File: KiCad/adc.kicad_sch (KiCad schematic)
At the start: 32 parts, among them U901 AP331, U902 74LVC2G53

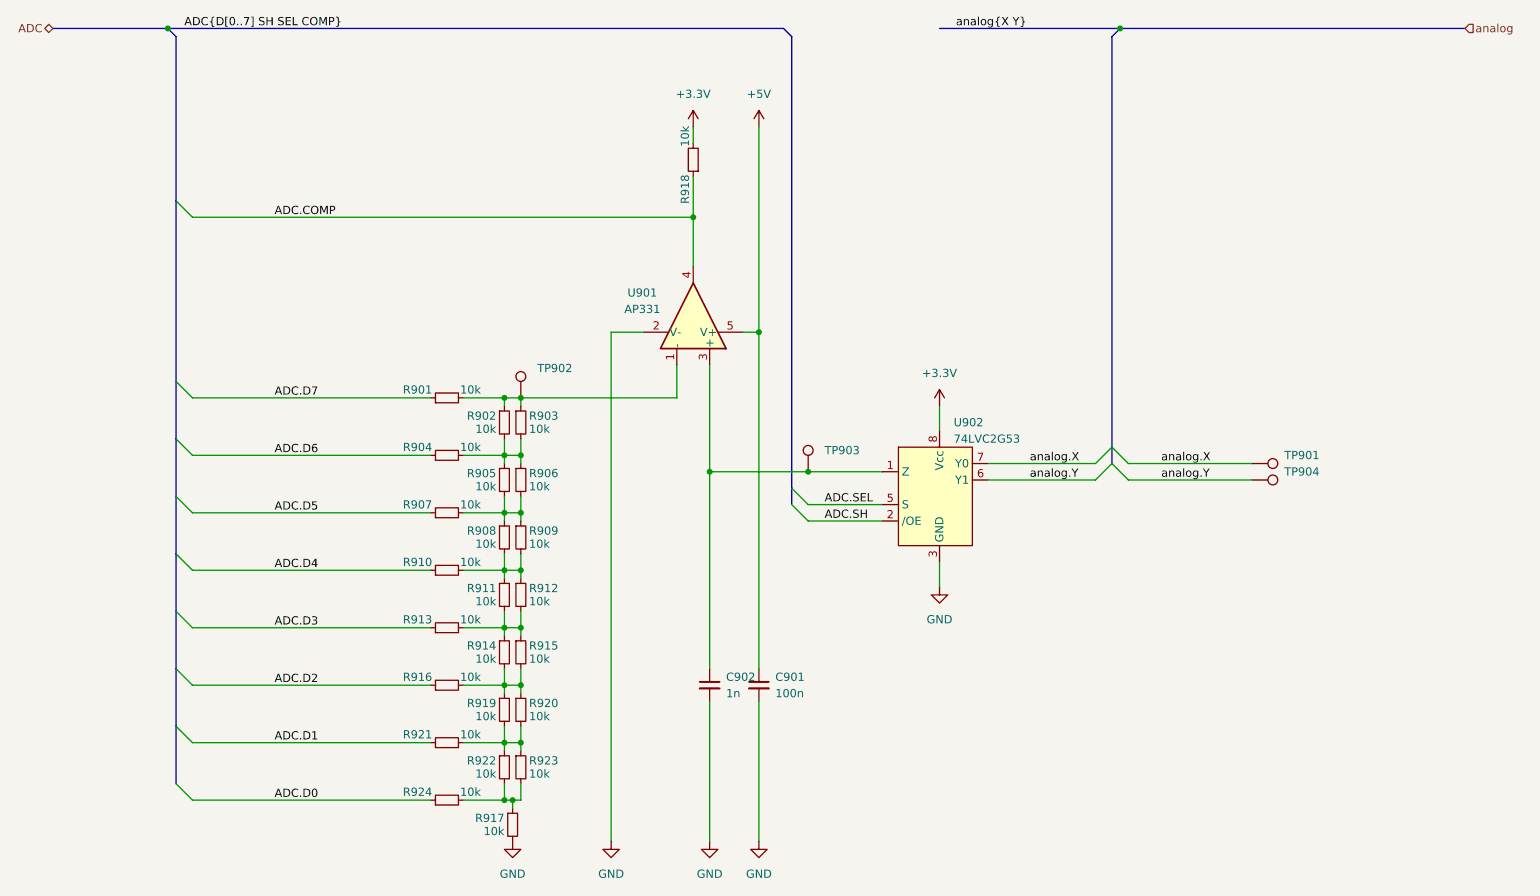
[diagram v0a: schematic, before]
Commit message: replaced SAR-ADC with Sigma-Delta-Converter
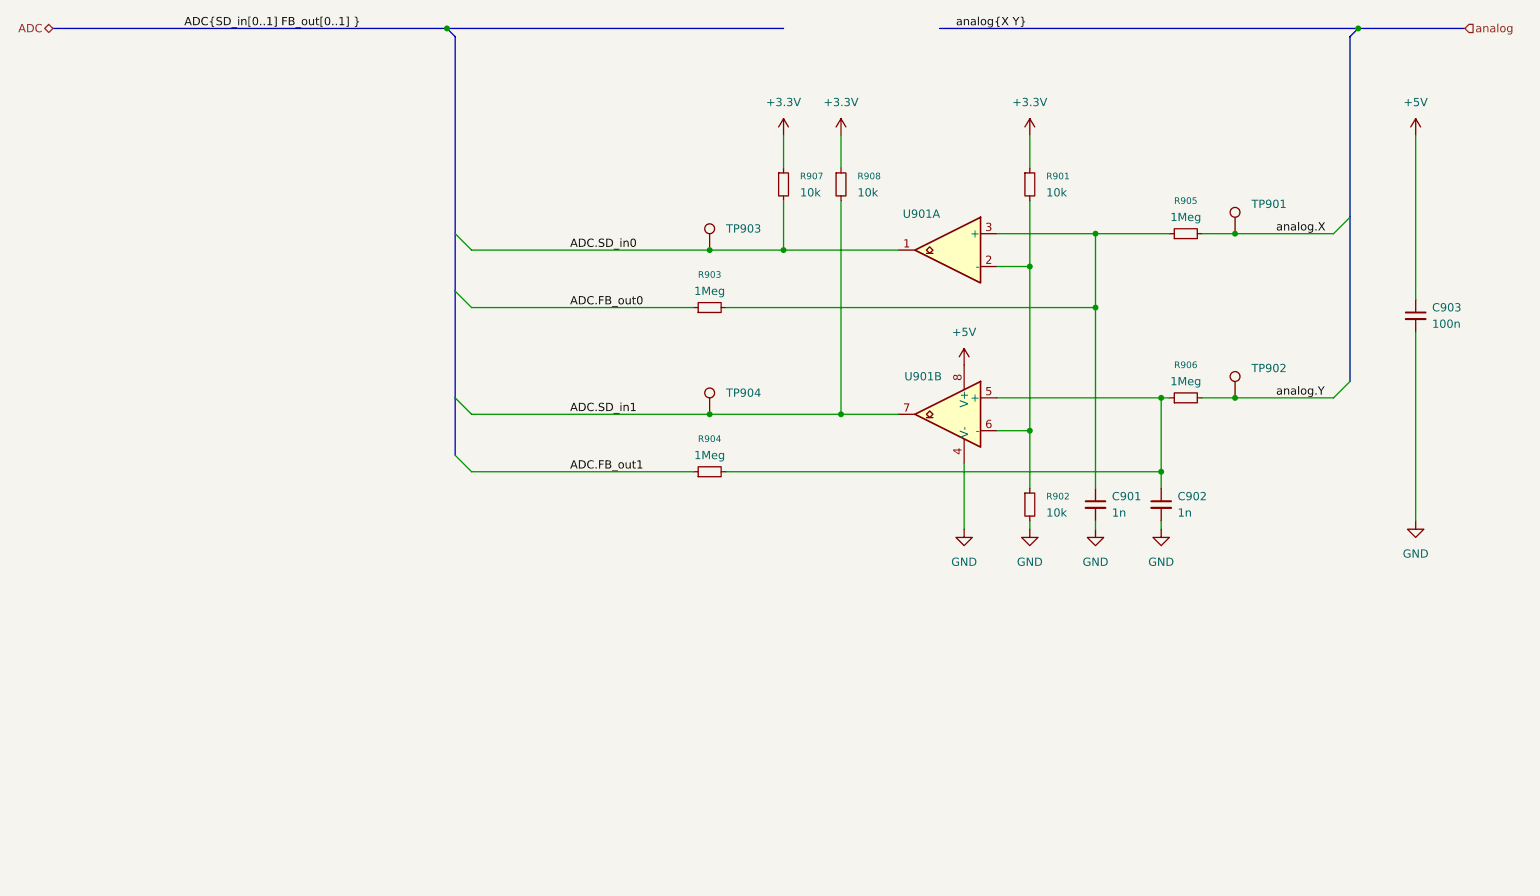
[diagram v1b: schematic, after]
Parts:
- removed R909, R910, R911, R912, R913, R914, R915, R916, R917, R918, R919, R920, R921, R922, R923, R924: 10k, Resistor_SMD:R_0402_1005Metric, symbol Device:R_Small
- removed U901: AP331, Package_TO_SOT_SMD:SOT-23-5, symbol Comparator:LM397
- removed U902: 74LVC2G53, Package_SO:VSSOP-8_2.4x2.1mm_P0.5mm, symbol FPGA-Devel:74LVC2G53
- added C903: 100n, Capacitor_SMD:C_0402_1005Metric, symbol Device:C_Small
- added U901: LM2903, Package_SO:VSSOP-8_3x3mm_P0.65mm, symbol Comparator:LM2903
- C901: value 100n -> 1n; Würth 885012205037 -> (none)
- C902: Würth 885012205025 -> (none)
- R901, R902, R907, R908: Würth 560112110020 -> (none)
- R903, R904, R905, R906: value 10k -> 1Meg; Würth 560112110020 -> (none)
- TP901, TP902, TP903, TP904: Würth - -> (none)
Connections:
- net ADC.D5 is gone; now on net +3.3V: R907.1
- net ADC.D7 is gone; now on net +3.3V: R901.1
- net +3.3V: now also R908.1
- net +5V: now also C903.1, U901.8 (V+); no longer C901.1
- net GND: now also R902.2, C903.2, U901.4 (V-)
- net analog.X: now also R905.2
- net analog.Y: now also R906.2, TP902.1; no longer TP904.1
- net at C902.1: now also R904.2, R906.1, U901.5 (+); no longer TP903.1
- net at R901.2, R902.1: now also U901.2 (-), U901.6 (-); no longer R903.1, TP902.1
- net ADC.SD_in1: now reaches R908.2
- net ADC.SD_in1: now also TP904.1, U901.7
- net ADC.D6 renamed ADC.FB_out1
- new net: C901.1, R903.2, R905.1, U901.3 (+)
- new net ADC.FB_out0: R903.1
- new net ADC.SD_in0: R907.2, TP903.1, U901.1

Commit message: Vorberitung für micro-SD
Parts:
- C901, C902: Würth (none) -> 885012005018
- C903: Würth (none) -> 885012205037
- R901, R902, R907, R908: Würth (none) -> 560112110020
- R903, R904, R905, R906: Würth (none) -> 560112110033
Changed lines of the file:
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@@
+			)
+		)
+		(property "Würth" "885012005018"
+			(at 200.66 124.46 0)
+			(effects
+				(font
+					(size 1.27 1.27)
+				)
+				(hide yes)
 			)
 		)
@@
 			)
 		)
+		(property "Würth" "560112110033"
+			(at 214.63 107.95 90)
+			(effects
+				(font
+					(size 1.27 1.27)
+				)
+				(hide yes)
+			)
+		)
 		(pin "2"
 		)
@@
 			)
 		)
+		(property "Würth" "885012005018"
+			(at 210.82 124.46 0)
+			(effects
+				(font
+					(size 1.27 1.27)
+				)
+				(hide yes)
+			)
+		)
 		(pin "2"
 		)
@@
 			)
 		)
+		(property "Würth" "560112110020"
+			(at 190.5 124.46 0)
+			(effects
+				(font
+					(size 1.27 1.27)
+				)
+				(hide yes)
+			)
+		)
 		(pin "2"
 		)
@@
 		(property "Description" "Resistor, small symbol"
 			(at 214.63 82.55 0)
+			(effects
+				(font
+					(size 1.27 1.27)
+				)
+				(hide yes)
+			)
+		)
+		(property "Würth" "560112110033"
+			(at 214.63 82.55 90)
 			(effects
 				(font
@@
 			)
 		)
+		(property "Würth" "560112110020"
+			(at 152.4 74.93 0)
+			(effects
+				(font
+					(size 1.27 1.27)
+				)
+				(hide yes)
+			)
+		)
 		(pin "2"
 		)
@@
 			)
 		)
+		(property "Würth" "885012205037"
+			(at 250.19 95.25 0)
+			(effects
+				(font
+					(size 1.27 1.27)
+				)
+				(hide yes)
+			)
+		)
 		(pin "2"
 		)
@@
 			)
 		)
+		(property "Würth" "560112110033"
+			(at 140.97 93.98 90)
+			(effects
+				(font
+					(size 1.27 1.27)
+				)
+				(hide yes)
+			)
+		)
 		(pin "2"
 		)
@@
 			)
 		)
+		(property "Würth" "560112110020"
+			(at 190.5 74.93 0)
+			(effects
+				(font
+					(size 1.27 1.27)
+				)
+				(hide yes)
+			)
+		)
 		(pin "2"
 		)
@@
 			)
 		)
+		(property "Würth" "560112110033"
+			(at 140.97 119.38 90)
+			(effects
+				(font
+					(size 1.27 1.27)
+				)
+				(hide yes)
+			)
+		)
 		(pin "2"
 		)
@@
 			(at 161.29 74.93 0)
 			(effects
+				(font
+					(size 1.27 1.27)
+				)
+				(hide yes)
+			)
+		)
+		(property "Würth" "560112110020"
+			(at 161.29 74.93 0)
+			(effects

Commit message: LEDs zur Visualisierung des ausgewählten FPGAs
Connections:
- net IntX: now reaches C901.1, R903.2, R905.1, U901.3 (+)
- net IntY: now reaches C902.1, R904.2, R906.1, U901.5 (+)
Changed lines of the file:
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@@
+		)
+	)
+	(label "IntX"
+		(at 203.2 82.55 0)
+		(effects
+			(font
+				(size 1.27 1.27)
+			)
+			(justify left bottom)
 		)
 	)
@@
 		(effects
 			(font
+				(size 1.27 1.27)
+			)
+			(justify left bottom)
+		)
+	)
+	(label "IntY"
+		(at 203.2 119.38 0)
+		(effects
+			(font

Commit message: minor touches
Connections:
- net ADC.FB_out0: now also TP903.1
- net ADC.FB_out1: now also TP904.1
- net ADC.SD_in0: no longer TP903.1
- net ADC.SD_in1: no longer TP904.1
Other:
- moved on the sheet: TP903, TP904
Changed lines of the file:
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@@
+	)
+	(junction
+		(at 135.89 119.38)
+		(diameter 0)
+		(color 0 0 0 0)
 	)
 	(junction
@@
 	)
 	(junction
-		(at 140.97 110.49)
-		(diameter 0)
-		(color 0 0 0 0)
-	)
-	(junction
-		(at 140.97 85.09)
-		(diameter 0)
-		(color 0 0 0 0)
-	)
-	(junction
 		(at 200.66 93.98)
 		(diameter 0)
@@
 	)
 	(junction
+		(at 135.89 93.98)
+		(diameter 0)
+		(color 0 0 0 0)
+	)
+	(junction
 		(at 200.66 82.55)
 		(diameter 0)
@@
 	(wire
 		(pts
-			(xy 140.97 110.49) (xy 161.29 110.49)
-		)
-		(stroke
-			(width 0)
-			(type default)
-		)
-	)
-	(wire
-		(pts
 			(xy 200.66 93.98) (xy 200.66 82.55)
 		)
@@
 	(wire
 		(pts
-			(xy 104.14 93.98) (xy 138.43 93.98)
+			(xy 104.14 93.98) (xy 135.89 93.98)
 		)
 		(stroke
@@
 		)
 	)
+	(wire
+		(pts
+			(xy 135.89 93.98) (xy 138.43 93.98)
+		)
+		(stroke
+			(width 0)
+			(type default)
+		)
+	)
 	(bus
 		(pts
@@
 	(wire
 		(pts
-			(xy 104.14 110.49) (xy 140.97 110.49)
+			(xy 104.14 110.49) (xy 161.29 110.49)
 		)
 		(stroke
@@
 	(wire
 		(pts
-			(xy 104.14 119.38) (xy 138.43 119.38)
+			(xy 104.14 119.38) (xy 135.89 119.38)
 		)
 		(stroke
@@
 	(wire
 		(pts
+			(xy 135.89 119.38) (xy 138.43 119.38)
+		)
+		(stroke
+			(width 0)
+			(type default)
+		)
+	)
+	(wire
+		(pts
 			(xy 200.66 127) (xy 200.66 128.27)
 		)
@@
 	(wire
 		(pts
-			(xy 104.14 85.09) (xy 140.97 85.09)
+			(xy 104.14 85.09) (xy 152.4 85.09)
 		)
 		(stroke
@@
 		(pts
 			(xy 185.42 113.03) (xy 190.5 113.03)
-		)
-		(stroke
-			(width 0)
-			(type default)
-		)
-	)
-	(wire
-		(pts
-			(xy 140.97 85.09) (xy 152.4 85.09)
 		)
 		(stroke
@@
 	(symbol
 		(lib_id "Connector:TestPoint")
-		(at 140.97 110.49 0)
+		(at 135.89 119.38 0)
 		(unit 1)
 		(body_style 1)
@@
 		(in_pos_files yes)
 		(dnp no)
-		(fields_autoplaced yes)
 		(property "Reference" "TP904"
-			(at 143.51 107.1879 0)
+			(at 132.588 121.158 0)
 			(show_name no)
 			(do_not_autoplace no)
@@
 		)
 		(property "Value" "TestPoint"
-			(at 143.51 108.4579 0)
+			(at 138.43 117.3479 0)
 			(hide yes)
 			(show_name no)
@@
 		)
 		(property "Footprint" "TestPoint:TestPoint_THTPad_D2.0mm_Drill1.0mm"
-			(at 146.05 110.49 0)
+			(at 140.97 119.38 0)
 			(hide yes)
 			(show_name no)
@@
 		)
 		(property "Datasheet" ""
-			(at 146.05 110.49 0)
+			(at 140.97 119.38 0)
 			(hide yes)
 			(show_name no)
@@
 		)
 		(property "Description" "test point"
-			(at 140.97 110.49 0)
+			(at 135.89 119.38 0)
 			(hide yes)
 			(show_name no)
@@
 	(symbol
 		(lib_id "Connector:TestPoint")
-		(at 140.97 85.09 0)
+		(at 135.89 93.98 0)
 		(unit 1)
 		(body_style 1)
@@
 		(in_pos_files yes)
 		(dnp no)
-		(fields_autoplaced yes)
 		(property "Reference" "TP903"
-			(at 143.51 81.7879 0)
+			(at 132.588 95.504 0)
 			(show_name no)
 			(do_not_autoplace no)
@@
 		)
 		(property "Value" "TestPoint"
-			(at 143.51 83.0579 0)
+			(at 138.43 91.9479 0)
 			(hide yes)
 			(show_name no)
@@
 		)
 		(property "Footprint" "TestPoint:TestPoint_THTPad_D2.0mm_Drill1.0mm"
-			(at 146.05 85.09 0)
+			(at 140.97 93.98 0)
 			(hide yes)
 			(show_name no)
@@
 		)
 		(property "Datasheet" ""
-			(at 146.05 85.09 0)
+			(at 140.97 93.98 0)
 			(hide yes)
 			(show_name no)
@@
 		)
 		(property "Description" "test point"
-			(at 140.97 85.09 0)
-			(hide yes)
-			(show_name no)
+			(at 135.89 93.98 0)
+			(hide yes)
+			(show_name no)
